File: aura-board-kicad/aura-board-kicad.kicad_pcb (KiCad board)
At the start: 2 copper layers, 70.5 x 53.3 mm, 16 parts, among them J1 Main Power, J2 PWM Outputs, J3 BB-UART0, J4 Attopilot, J5 GPS, J6 SBUS, J7 Telemetry, U1 TSR2-2450, U2 PocketBeagle, U3 Teensy-3.2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

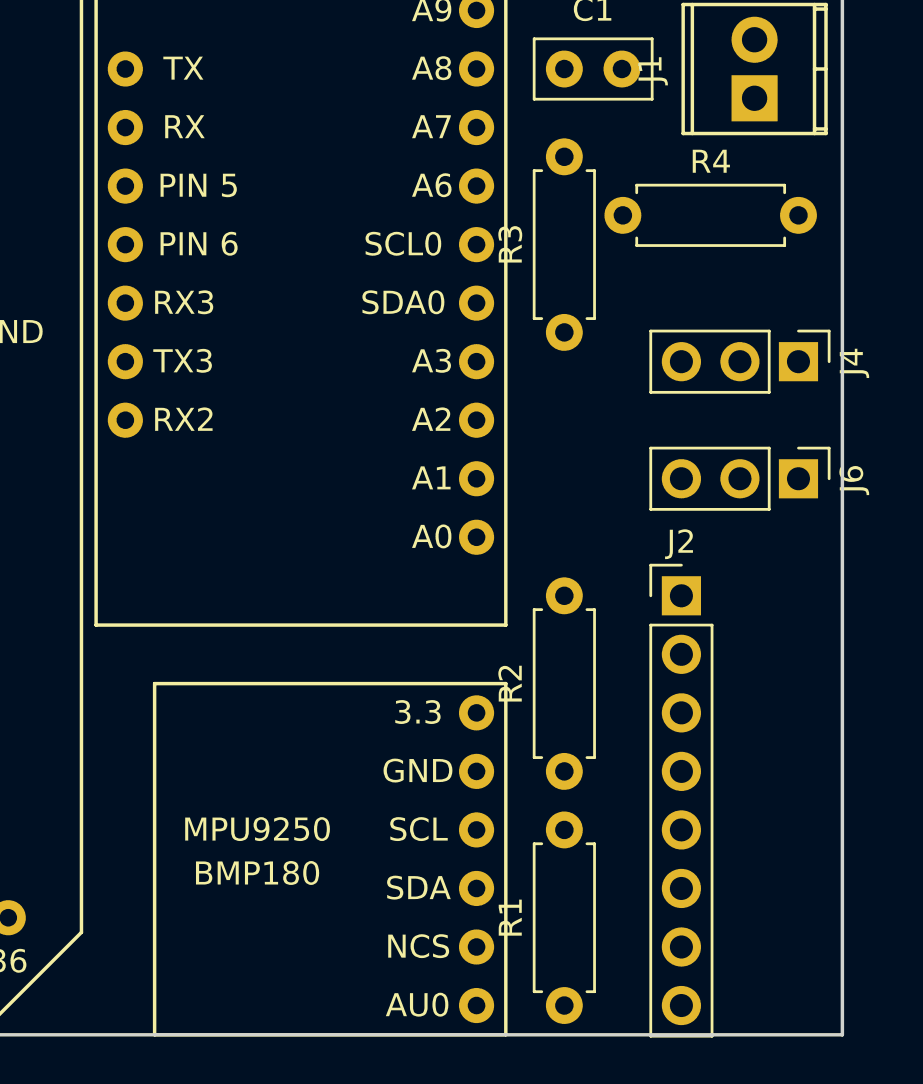
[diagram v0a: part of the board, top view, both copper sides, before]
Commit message: Fix a wrong units issue.
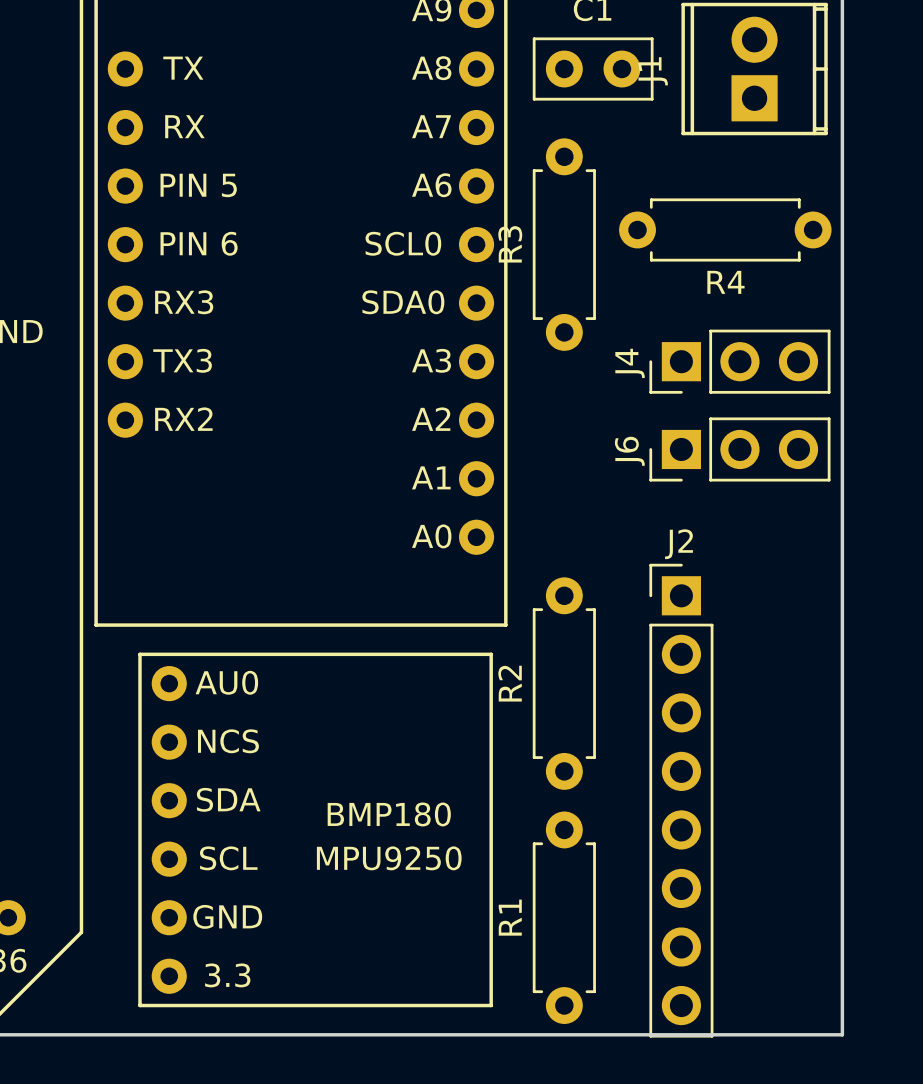
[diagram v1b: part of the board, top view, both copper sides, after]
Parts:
- moved U4 14.0 mm to (76.8, 101.6), turned to 180 degrees
- moved R4 8.28 mm to (98.4, 67.9), turned to 180 degrees
- moved J6 5.24 mm to (92.7, 77.5), turned to 90 degrees
- moved J4 5.08 mm to (92.7, 73.7), turned to 90 degrees
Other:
- net class Default: clearance 6.35 -> 0.25; trace_width 6.35 -> 25; via_dia 15.24 -> 0.6; via_drill 10.16 -> 0.4
- rule trace_clearance: 6.35 -> 0.25
- rule trace_min: 6.35 -> 0.25

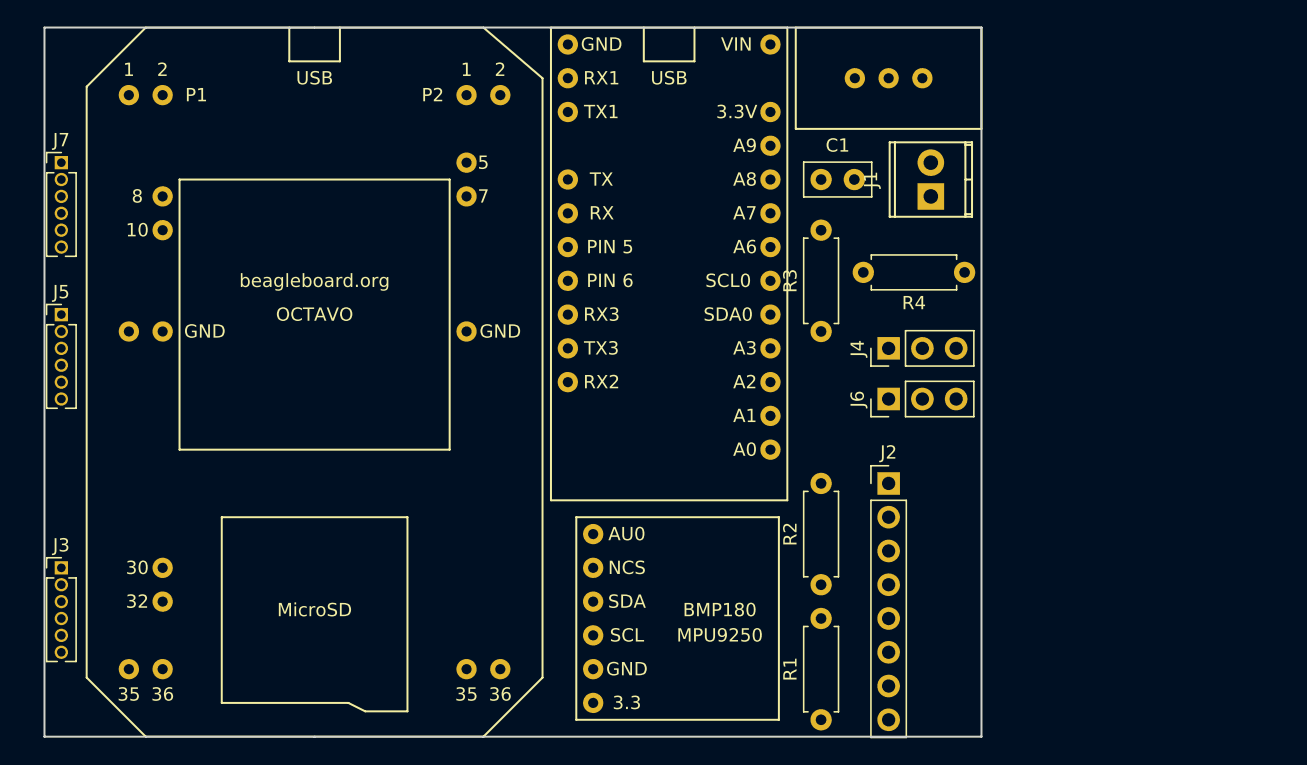
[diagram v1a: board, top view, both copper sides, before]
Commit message: Start adding a few easy traces.
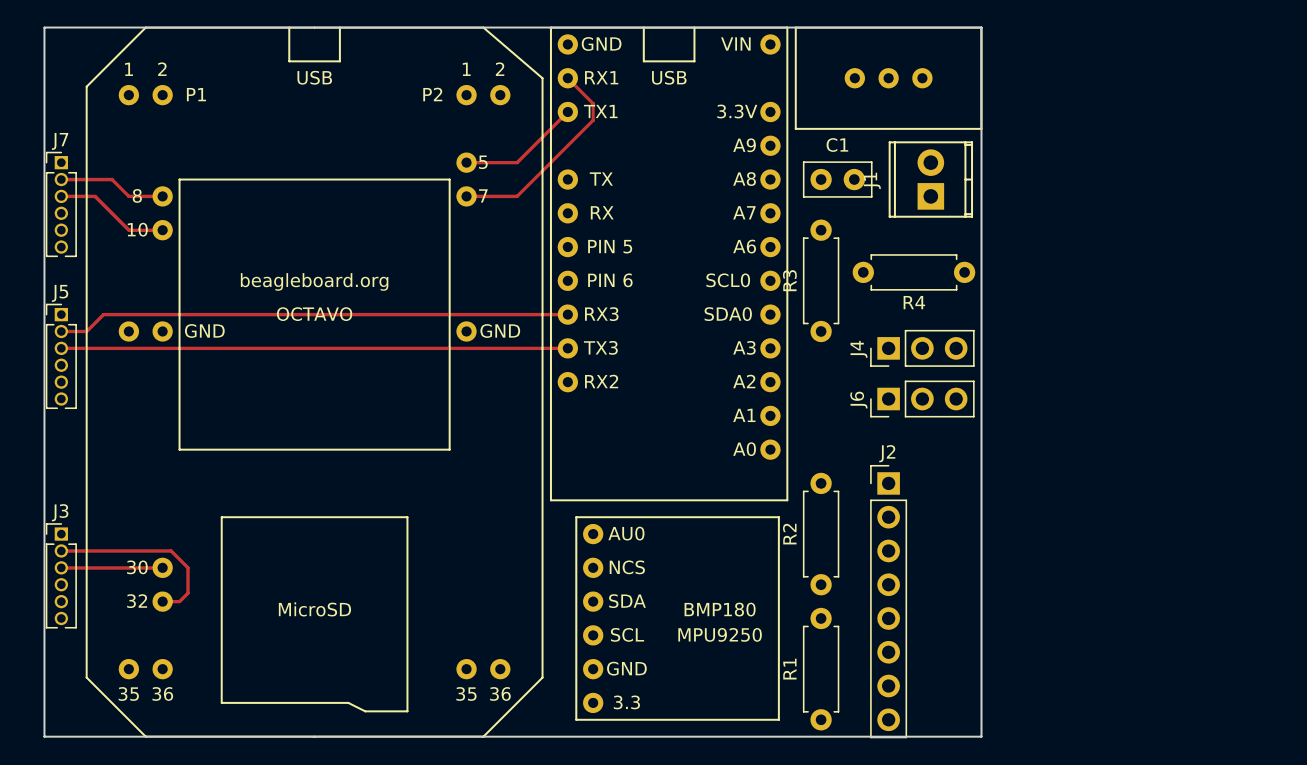
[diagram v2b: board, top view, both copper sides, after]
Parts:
- moved J3 2.54 mm to (30.5, 87.6)
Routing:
- net /GPS_RX: track 0.00 -> 38.6 mm
- net /GPS_TX: track 0.00 -> 38.1 mm
- net /UART1_RX: track 0.00 -> 15.9 mm
- net /UART0_RX: track 0.00 -> 14.1 mm
- net /UART1_TX: track 0.00 -> 9.20 mm
- net /UART2_TX: track 0.00 -> 8.67 mm
- net /UART2_RX: track 0.00 -> 8.15 mm
- net /UART0_TX: track 0.00 -> 7.62 mm
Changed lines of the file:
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@@
   (general
     (links 53)
-    (no_connects 53)
-    (area 26.297429 47.231 101.51488 105.059)
+    (no_connects 45)
+    (area 26.301429 47.235 101.51088 105.055)
     (thickness 1.6)
     (drawings 4)
-    (tracks 0)
+    (tracks 22)
     (zones 0)
     (modules 16)
@@
   )
   (setup
-    (last_trace_width 25)
+    (last_trace_width 0.25)
+    (user_trace_width 0.25)
+    (user_trace_width 0.5)
     (trace_clearance 0.25)
     (zone_clearance 0.508)
@@
   )
   (module Pin_Headers:Pin_Header_Straight_1x06_Pitch1.27mm (layer F.Cu)
-    (at 30.48 90.17)
+    (at 30.48 87.63)
     (descr "Through hole straight pin header, 1x06, 1.27mm pitch, single row")
     (tags "Through hole pin header THT 1x06 1.27mm single row")
@@
   (gr_line (start 29.21 102.87) (end 99.695 102.87) (angle 90) (layer Edge.Cuts) (width 0.15))
   (gr_line (start 29.21 49.53) (end 29.21 102.87) (angle 90) (layer Edge.Cuts) (width 0.15))
+  (segment (start 38.1 92.71) (end 39.37 92.71) (width 0.25) (layer F.Cu) (net 12) (status 400000))
+  (segment (start 38.735 88.9) (end 30.48 88.9) (width 0.25) (layer F.Cu) (net 12) (status 800000))
+  (segment (start 40.005 90.17) (end 38.735 88.9) (width 0.25) (layer F.Cu) (net 12))
+  (segment (start 40.005 92.075) (end 40.005 90.17) (width 0.25) (layer F.Cu) (net 12))
+  (segment (start 39.37 92.71) (end 40.005 92.075) (width 0.25) (layer F.Cu) (net 12))
+  (segment (start 38.1 90.17) (end 30.48 90.17) (width 0.25) (layer F.Cu) (net 13) (status C00000))
+  (segment (start 68.58 71.12) (end 33.655 71.12) (width 0.25) (layer F.Cu) (net 17))
+  (segment (start 32.385 72.39) (end 30.48 72.39) (width 0.25) (layer F.Cu) (net 17))
+  (segment (start 33.655 71.12) (end 32.385 72.39) (width 0.25) (layer F.Cu) (net 17))
+  (segment (start 68.58 73.66) (end 30.48 73.66) (width 0.25) (layer F.Cu) (net 18))
+  (segment (start 38.1 62.23) (end 35.56 62.23) (width 0.25) (layer F.Cu) (net 21))
+  (segment (start 34.29 60.96) (end 30.48 60.96) (width 0.25) (layer F.Cu) (net 21))
+  (segment (start 35.56 62.23) (end 34.29 60.96) (width 0.25) (layer F.Cu) (net 21))
+  (segment (start 38.1 64.77) (end 35.56 64.77) (width 0.25) (layer F.Cu) (net 22))
+  (segment (start 33.02 62.23) (end 30.48 62.23) (width 0.25) (layer F.Cu) (net 22))
+  (segment (start 35.56 64.77) (end 33.02 62.23) (width 0.25) (layer F.Cu) (net 22))
+  (segment (start 60.96 59.69) (end 64.77 59.69) (width 0.25) (layer F.Cu) (net 26) (status 400000))
+  (segment (start 64.77 59.69) (end 68.58 55.88) (width 0.25) (layer F.Cu) (net 26) (status 800000))
+  (segment (start 60.96 62.23) (end 64.77 62.23) (width 0.25) (layer F.Cu) (net 27) (status 400000))
+  (segment (start 70.485 55.245) (end 68.58 53.34) (width 0.25) (layer F.Cu) (net 27) (status 800000))
+  (segment (start 70.485 56.515) (end 70.485 55.245) (width 0.25) (layer F.Cu) (net 27))
+  (segment (start 64.77 62.23) (end 70.485 56.515) (width 0.25) (layer F.Cu) (net 27))
 )

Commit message: Shuffle PWM assignment on teensy (schematic) to make tracerouting more convenient. Work on trace routing. (Still need to set up a ground plane and create the power bus.)
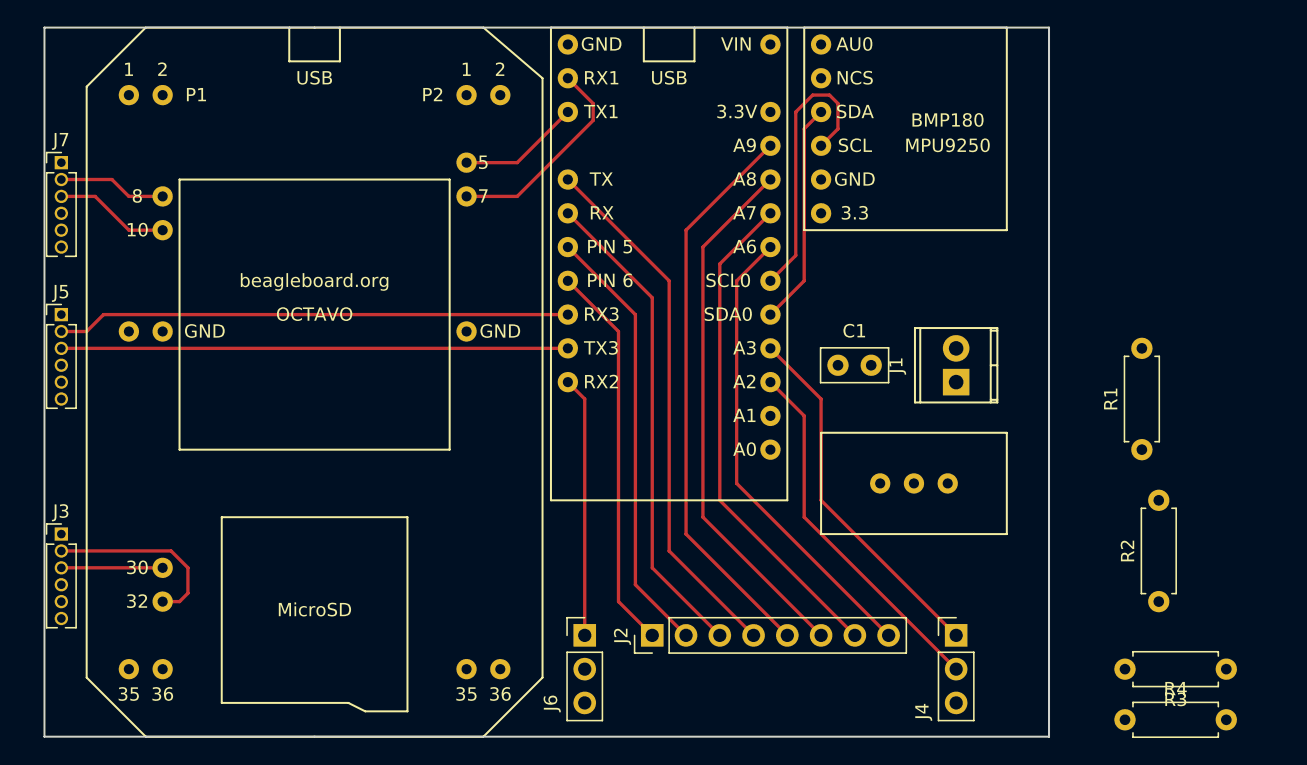
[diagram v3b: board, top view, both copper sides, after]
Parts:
- moved U4 40.6 mm to (94.0, 64.8)
- moved R3 39.7 mm to (118.1, 97.8), turned to 180 degrees
- moved U1 38.1 mm to (94.6, 87.6), turned to 180 degrees
- moved R4 35.8 mm to (110.5, 101.6), turned to 0 degrees
- moved R1 31.5 mm to (111.8, 81.3)
- moved J6 29.0 mm to (69.8, 95.2), turned to 0 degrees
- moved R2 25.4 mm to (113.0, 92.7)
- moved J4 22.2 mm to (97.8, 95.2), turned to 0 degrees
- moved J2 21.1 mm to (74.9, 95.2), turned to 90 degrees
- moved J1 14.1 mm to (97.8, 76.2)
- moved C1 14.0 mm to (88.9, 74.9)
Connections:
- U3 pad 5: /PWM1 -> /PWM4
- U3 pad 6: /PWM2 -> /PWM3
- U3 pad 7: /PWM3 -> /PWM2
- U3 pad 8: /PWM4 -> /PWM1
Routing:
- net /PWM5: track 0.00 -> 42.6 mm
- net /PWM4: track 0.00 -> 40.1 mm
- net /PWM6: track 0.00 -> 40.1 mm
- net /PWM7: track 0.00 -> 37.5 mm
- net /PWM3: track 0.00 -> 36.5 mm
- net /PWM8: track 0.00 -> 35.0 mm
- net /PWM2: track 0.00 -> 32.9 mm
- net /PWM1: track 0.00 -> 29.3 mm
- net /ATTO_VOLTS: track 0.00 -> 27.4 mm
- net /ATTO_AMPS: track 0.00 -> 27.4 mm
- net /I2C0_SCL: track 0.00 -> 21.2 mm
- net /SBUS_RX: track 0.00 -> 19.6 mm
- net /I2C0_SDA: track 0.00 -> 16.8 mm
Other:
- board size 70.5 x 53.3 mm -> 75.6 x 53.3 mm

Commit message: Add a ground plane.
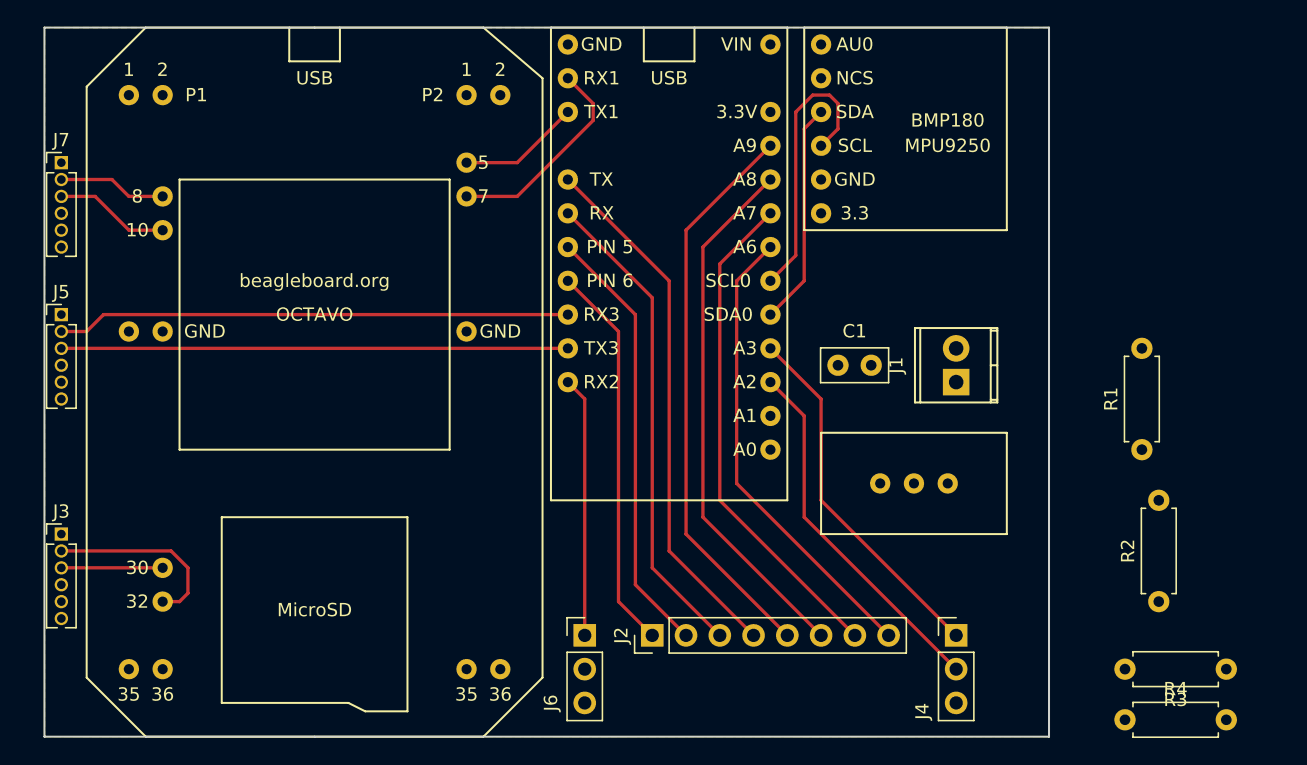
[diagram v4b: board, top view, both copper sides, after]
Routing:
- added copper zone on B.Cu, net GND
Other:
- net class Default: clearance 0.25 -> 0.1524; trace_width 25 -> 0.1524; via_dia 0.6 -> 0.6858; via_drill 0.4 -> 0.3302
- rule pad_to_mask_clearance: 0.2 -> 0.0508
- rule trace_clearance: 0.25 -> 0.1524
- rule trace_min: 0.25 -> 0.1524
- rule via_min_drill: 0.3 -> 0.3302
- rule via_min_size: 0.4 -> 0.6858
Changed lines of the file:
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@@
   (general
     (links 53)
-    (no_connects 32)
-    (area 26.301429 49.005 119.465001 105.035)
+    (no_connects 17)
+    (area 26.399029 49.1026 119.367401 104.9374)
     (thickness 1.6)
     (drawings 4)
@@
   )
   (setup
-    (last_trace_width 0.25)
-    (user_trace_width 0.25)
-    (user_trace_width 0.5)
-    (trace_clearance 0.25)
+    (last_trace_width 0.1524)
+    (user_trace_width 0.254)
+    (user_trace_width 0.508)
+    (user_trace_width 0.635)
+    (trace_clearance 0.1524)
     (zone_clearance 0.508)
     (zone_45_only no)
-    (trace_min 0.25)
+    (trace_min 0.1524)
     (segment_width 0.2)
     (edge_width 0.15)
-    (via_size 0.6)
-    (via_drill 0.4)
-    (via_min_size 0.4)
-    (via_min_drill 0.3)
-    (uvia_size 0.3)
-    (uvia_drill 0.1)
+    (via_size 0.6858)
+    (via_drill 0.3302)
+    (via_min_size 0.6858)
+    (via_min_drill 0.3302)
+    (uvia_size 0.6858)
+    (uvia_drill 0.3302)
     (uvias_allowed no)
     (uvia_min_size 0)
@@
     (pad_size 1.524 1.524)
     (pad_drill 0.762)
-    (pad_to_mask_clearance 0.2)
+    (pad_to_mask_clearance 0.0508)
     (aux_axis_origin 0 0)
     (visible_elements FFFFFF7F)
@@
   (net 32 "Net-(U4-Pad6)")
   (net_class Default "This is the default net class."
-    (clearance 0.25)
-    (trace_width 25)
-    (via_dia 0.6)
-    (via_drill 0.4)
-    (uvia_dia 0.3)
-    (uvia_drill 0.1)
+    (clearance 0.1524)
+    (trace_width 0.1524)
+    (via_dia 0.6858)
+    (via_drill 0.3302)
+    (uvia_dia 0.6858)
+    (uvia_drill 0.3302)
     (add_net +3V3)
     (add_net +5V)
@@
   (segment (start 88.9 55.245) (end 88.265 54.61) (width 0.25) (layer F.Cu) (net 29))
   (segment (start 88.9 57.15) (end 88.9 55.245) (width 0.25) (layer F.Cu) (net 29))
+  (zone (net 2) (net_name GND) (layer B.Cu) (hatch edge 0.508)
+    (connect_pads (clearance 0.508))
+    (min_thickness 0.254)
+    (fill yes (arc_segments 16) (thermal_gap 0.508) (thermal_bridge_width 0.508))
+    (polygon
+      (pts
+        (xy 104.775 102.87) (xy 29.21 102.87) (xy 29.21 49.53) (xy 104.775 49.53)
+      )
+    )
+  )
 )
